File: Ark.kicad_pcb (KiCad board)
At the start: 2 copper layers, 71.9 x 89.1 mm, 109 parts, among them P1 USB_OTG, P2 USB_OTG, P3 40_Pin_LCD_Out, P4 6_Pin_Touch_In, Q1 MMUN2133LT1G, SW1 SW_PUSH_SMALL_H, SW2 SW_PUSH_SMALL_H, SW3 SW_PUSH_SMALL_H, SW4 SW_PUSH_SMALL_H, SW5 SW_PUSH_SMALL_H, SW6 SW_PUSH_SMALL_H, U1 PAM2306AYPKE, U2 AP7115-25SEG, U3 DDR2_SODIMM_CM_3_Lite, U4 1040310811, U5 FAN5333BSX, U6 TPS61090RSAR, U7 MCP73871, U8 SPDT_switch

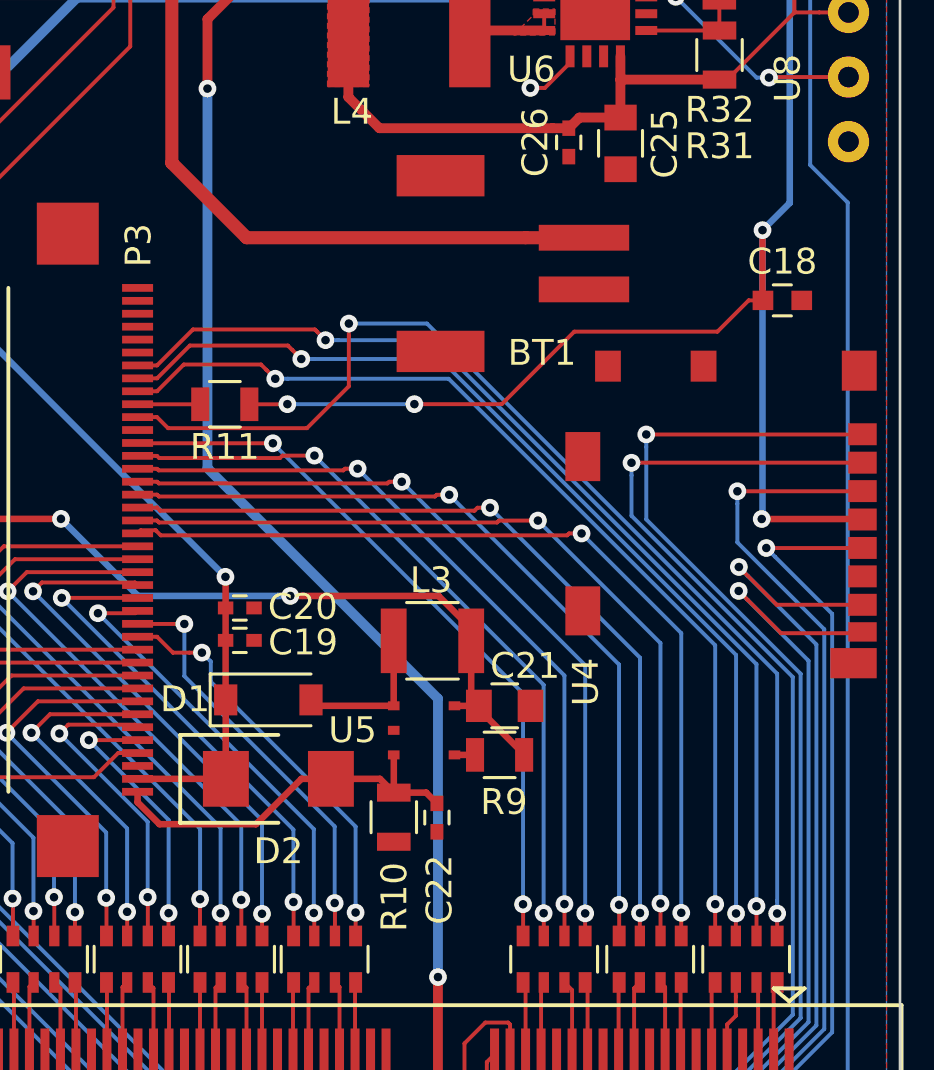
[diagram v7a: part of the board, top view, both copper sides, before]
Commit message: Fixed battery connector problem
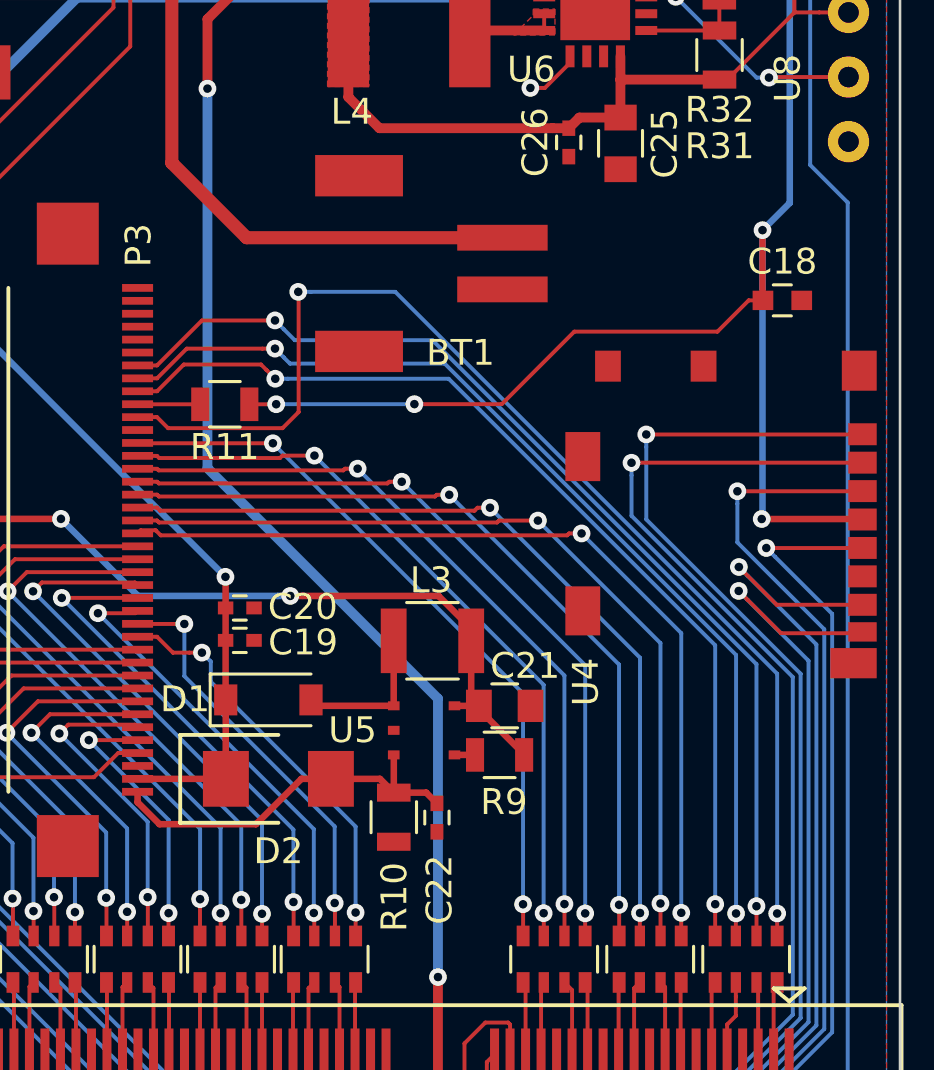
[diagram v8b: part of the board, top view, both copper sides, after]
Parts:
- moved BT1 3.15 mm to (157.5, 102.5)
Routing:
- net Net-(BT1-Pad1): track 59.4 -> 56.2 mm
- net Net-(P3-Pad30): track 43.8 -> 46.1 mm
